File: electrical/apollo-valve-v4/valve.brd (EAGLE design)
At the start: 160 x 100 mm, 42 parts, among them J1 VALVE2, J2 VALVE1, J7 455-1750-1-ND, U1 DRV8806-SSOP, U2 DRV8806-SSOP, U3 TPS54202

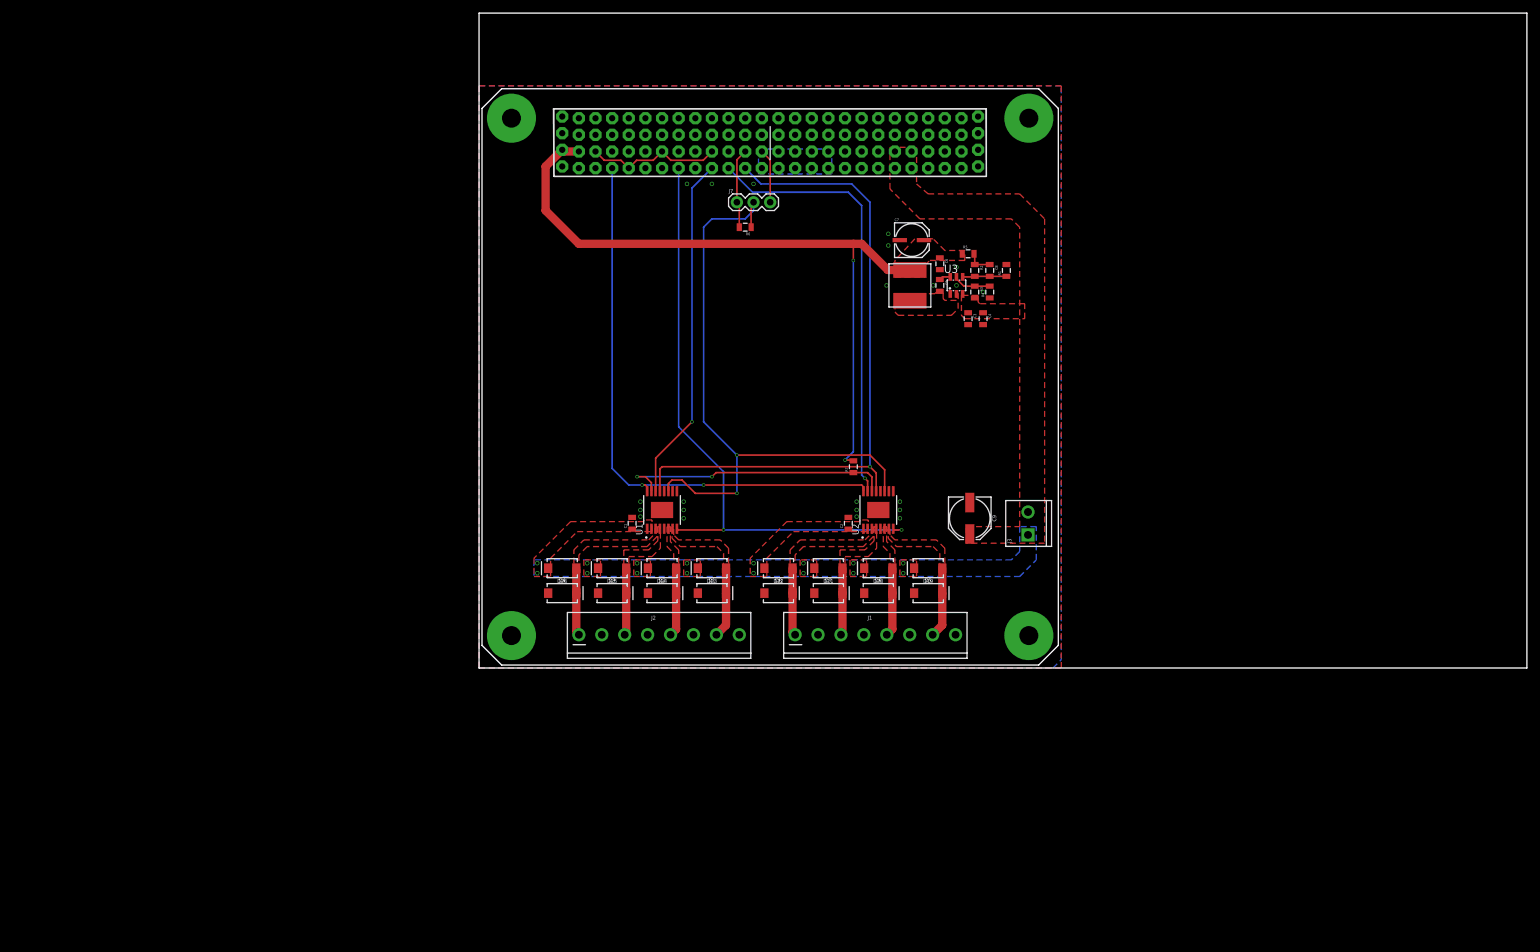
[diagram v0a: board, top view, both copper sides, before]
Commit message: Add stepper drivers to the valve board schematic. No guarantee that they fit, but if they do not another board can be made.
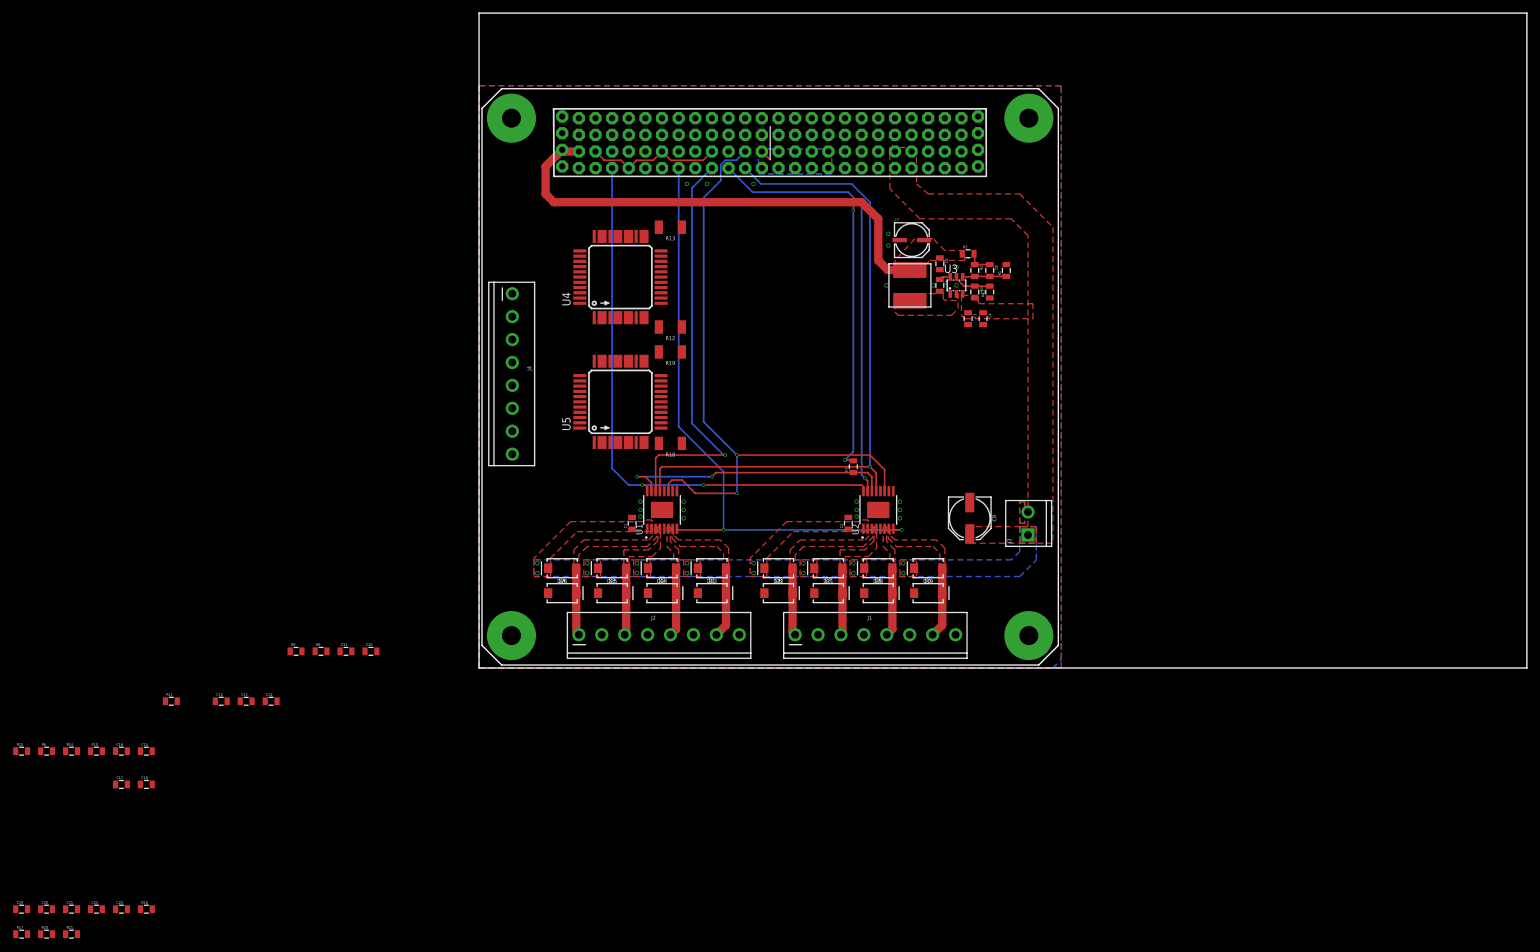
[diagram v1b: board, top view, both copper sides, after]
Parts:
- removed J7: 455-1750-1-ND, SparkFun-Connectors:1X03
- added C10, C11, C13, C14, C17, C18, C20, C21: 0.1u, apollo-ctrl-v4:0805
- added C12, C19: 10u, apollo-ctrl-v4:0805
- added C15, C16, C22, C23: 0.01u, apollo-ctrl-v4:0805
- added J4: STEP, SparkFun-Connectors:SCREWTERMINAL-3.5MM-8
- added R10, R14, R20, R21: 22, apollo-ctrl-v4:0805
- added R11: 13.3K, apollo-ctrl-v4:0805
- added R12, R13, R18, R19: 0.1, SparkFun-Resistors:1210
- added R15, R16, R17, R8, R9: 100K, apollo-ctrl-v4:0805
- added U4, U5: TMC2660, apollo-ctrl-v4:TMC2660
- R3: value 680K -> 499K
- R4: value 120K -> 82K
- moved R6 133.4 mm to (-66.0, -12.7), turned to 0 degrees
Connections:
- removed net LCS: J7.2, R6.1, U1.11, U2.11
- new net +12V: C12.1, C13.1, C14.1, C19.1, C20.1, C21.1, U4.30, U4.35, U4.36, U4.4, U5.30, U5.35, U5.36, U5.4
- new net +3V3: C11.1, C18.1, R15.2, R6.2, U$1.P$1, U4.40, U5.40
- new net 5VOUT1: C10.1, U4.13
- new net 5VOUT2: C17.1, U5.13
- new net BRA1: R10.2, R12.2, U4.9
- new net BRA2: R18.2, R20.2, U5.9
- new net BRB1: R13.2, R14.2, U4.25
- new net BRB2: R19.2, R21.2, U5.25
- new net DIR1: R8.2, U4.41
- new net DIR2: R16.2, U5.41
- new net RESET: R11.1, U1.9, U2.9
- new net S1A: J4.4, U4.2, U4.7
- new net S1B: J4.3, U4.10, U4.5
- new net S1C: J4.2, U4.26, U4.31
- new net S1D: J4.1, U4.23, U4.28
- new net S2A: J4.8, U5.2, U5.7
- new net S2B: J4.7, U5.10, U5.5
- new net S2C: J4.6, U5.26, U5.31
- new net S2D: J4.5, U5.23, U5.28
- new net SRA1: C15.1, R10.1, U4.12
- new net SRA2: C22.1, R20.1, U5.12
- new net SRB1: C16.1, R14.1, U4.22
- new net SRB2: C23.1, R21.1, U5.22
- new net STEP1: R9.2, U4.42
- new net STEP2: R17.2, U5.42
- net !LOE!: now also U4.19, U5.19
- net CIDO: now also U4.14, U5.14
- net CODI: now also U4.15, U5.15
- net CS1: now also U1.11, U2.11; no longer J7.1, R6.2
- net CS2: now also R6.1, U4.18; no longer J7.3
- net CS3: now also R15.1, U5.18
- net GND: now also C10.2, C11.2, C12.2, C13.2, C14.2, C15.2, C16.2, C17.2, C18.2, C19.2, C20.2, C21.2, C22.2, C23.2, R11.2, R12.1, R13.1, R16.1, R17.1, R18.1, R19.1, R8.1, R9.1, U4.17, U4.21, U4.39, U4.43, U4.44, U5.17, U5.21, U5.39, U5.43, U5.44
- net SCK: now also U4.16, U5.16
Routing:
- net LCS: track 96.1 -> 0.00 mm, vias 2 -> 0
- net CS1: track 12.2 -> 96.2 mm, vias 0 -> 2
- net CODI: track 52.9 -> 63.2 mm
- net +5V: track 107.2 -> 115.8 mm
- net CS2: track 8.28 -> 1.80 mm

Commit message: Remove the Trinamics bipolar stepper drivers and add unipolar stepper drivers instead (as the motors are cheaper and more available).
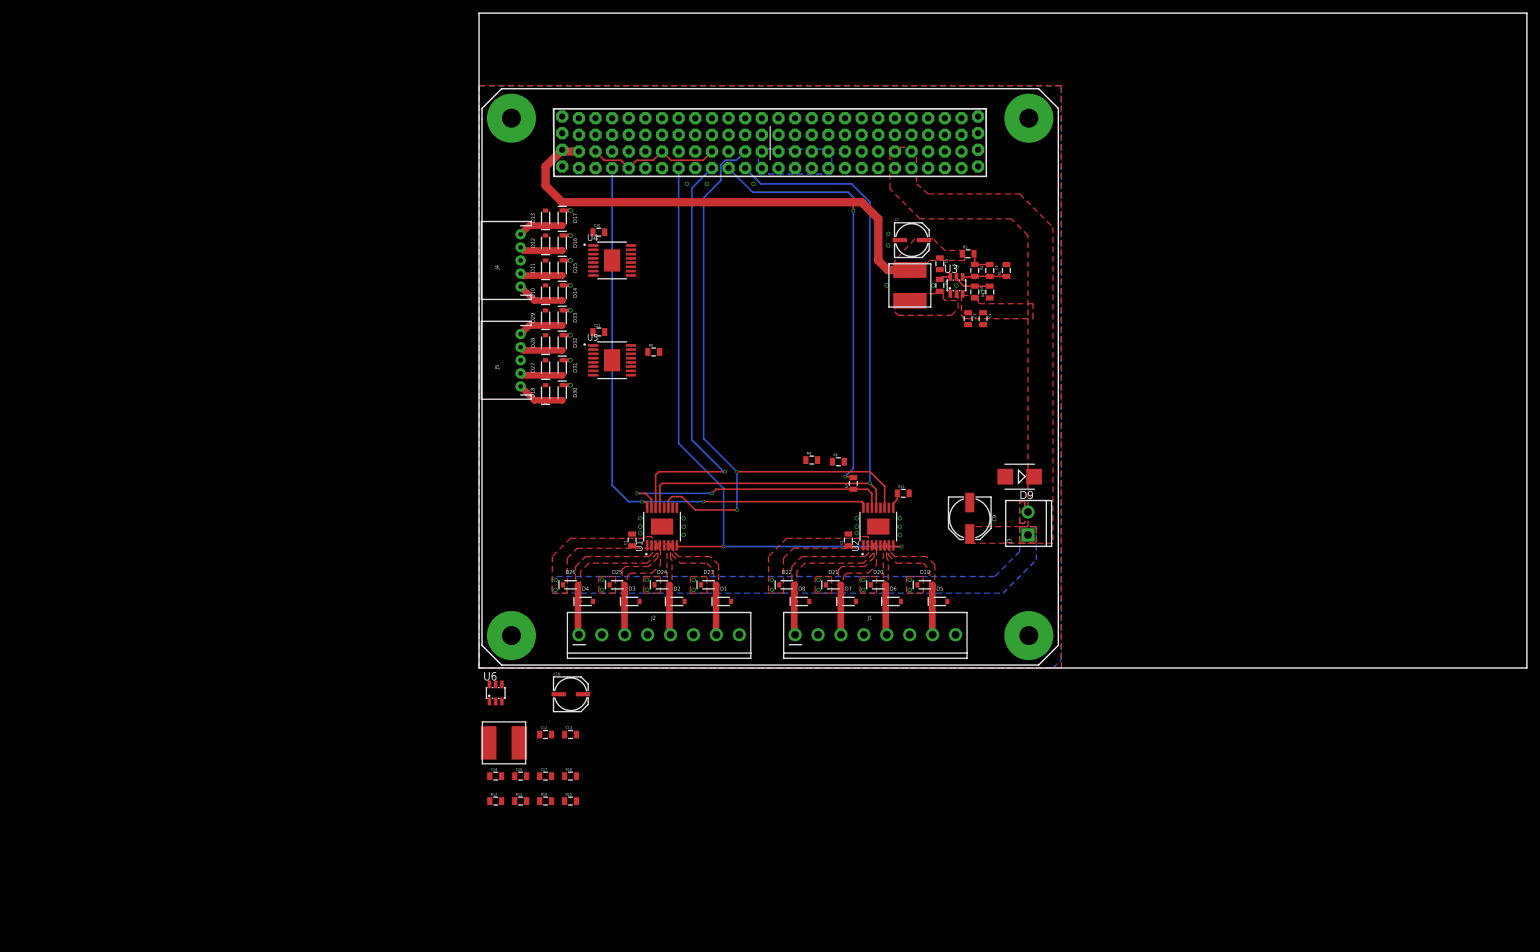
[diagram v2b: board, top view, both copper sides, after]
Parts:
- removed C18, C20, C21: 0.1u, apollo-ctrl-v4:0805
- removed C19: 10u, apollo-ctrl-v4:0805
- removed C22, C23: 0.01u, apollo-ctrl-v4:0805
- removed R16, R17: 100K, apollo-ctrl-v4:0805
- removed R18, R19: 0.1, SparkFun-Resistors:1210
- removed R20, R21: 22, apollo-ctrl-v4:0805
- added D10, D11, D12, D13, D14, D15, D16, D17, D18, D27, D28, D29, D30, D31, D32, D33: BAT46, SparkFun-DiscreteSemi:SOD-323
- added D9: SMBJ24A, diode:SMB
- added J5: S2, SparkFun-Connectors:JST-5-PTH
- added L2: VLS6045EX-220M, apollo-ctrl-v4:VLS6045EX
- added U6: TPS54202, apollo-ctrl-v4:SOT23-6L
- C12: value 10u -> 0.1u
- C13: value 0.1u -> 10u
- C15: value 0.01u -> 22u
- C16: value 0.01u -> 47u; device apollo-ctrl-v4:0805 -> apollo-ctrl-v4:PANASONIC_C
- C17: value 0.1u -> 100p
- D1, D19, D2, D20, D21, D22, D23, D24, D25, D26, D3, D4, D5, D6, D7, D8: value B340A -> BAT46; device SparkFun-DiscreteSemi:SMA-DIODE -> SparkFun-DiscreteSemi:SOD-323
- J4: value STEP -> S1; device SparkFun-Connectors:SCREWTERMINAL-3.5MM-8 -> SparkFun-Connectors:JST-5-PTH
- L1: value VLS6045EX-H -> VLS6045EX-150M
- R10: value 22 -> 5.23K
- R11: value 13.3K -> 2.2K
- R12: value 0.1 -> 100K; device SparkFun-Resistors:1210 -> apollo-ctrl-v4:0805
- R13: value 0.1 -> 499K; device SparkFun-Resistors:1210 -> apollo-ctrl-v4:0805
- R14: value 22 -> 82K
- R15: value 100K -> 49.9
- R6, R7, R8: value 100K -> 2.2K
- R9: value 100K -> EMPTY
- U4, U5: value TMC2660 -> DRV8806-SSOP; device apollo-ctrl-v4:TMC2660 -> apollo-ctrl-v4:SOP65P640X120-17N
- moved R6 128.7 mm to (54.9, 31.5)
- moved R11 116.2 mm to (64.8, 26.7)
- moved R13 90.6 mm to (6.35, -20.3), turned to 0 degrees
- moved R15 84.2 mm to (14.0, -20.3)
- moved R9 84.0 mm to (50.8, 31.8)
- moved R12 77.1 mm to (2.54, -20.3), turned to 0 degrees
- moved C10 72.9 mm to (18.3, 66.5)
- moved R14 72.8 mm to (10.2, -20.3)
- moved R10 72.5 mm to (14.0, -16.5)
- moved C16 69.2 mm to (14.0, -3.81)
- moved R8 68.3 mm to (26.7, 48.3)
- moved C17 64.8 mm to (10.2, -16.5)
- moved C11 62.2 mm to (18.3, 51.3)
- moved C15 57.3 mm to (6.35, -16.5)
- moved C13 49.8 mm to (14.0, -10.2)
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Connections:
- net VEN renamed VEN1
- removed net 5VOUT1: C10.1, U4.13
- removed net 5VOUT2: C17.1, U5.13
- removed net BRA1: R10.2, R12.2, U4.9
- removed net BRA2: R18.2, R20.2, U5.9
- removed net BRB1: R13.2, R14.2, U4.25
- removed net BRB2: R19.2, R21.2, U5.25
- removed net DIR1: R8.2, U4.41
- removed net DIR2: R16.2, U5.41
- removed net SRA1: C15.1, R10.1, U4.12
- removed net SRA2: C22.1, R20.1, U5.12
- removed net SRB1: C16.1, R14.1, U4.22
- removed net SRB2: C23.1, R21.1, U5.22
- removed net STEP1: R9.2, U4.42
- removed net STEP2: R17.2, U5.42
- new net BOOT2: C14.1, U6.6
- new net CIDO2: R6.1, R9.2, U2.15, U4.14
- new net CIDO3: R8.1, U4.15, U5.14
- new net FB2: C17.2, R10.1, R12.2, U6.4
- new net FF2: C17.1, R12.1, R15.2
- new net SW2: C14.2, L2.1, U6.2
- new net VEN2: R13.1, R14.2, U6.5
- net !FAULT!: now also U4.16, U5.16
- net !LOE!: now also U4.8, U5.8; no longer U4.19, U5.19
- net +12V: now also C10.1, C11.1, C15.1, C16.+, D14.C, D15.C, D16.C, D17.C, D30.C, D31.C, D32.C, D33.C, L2.2, R15.1, U4.1, U4.2, U5.1, U5.2; no longer C12.1, C13.1, C14.1, C19.1, C20.1, C21.1, U4.30, U4.35, U4.36, U4.4, U5.30, U5.35, U5.36, U5.4
- net +24V: now also C12.1, C13.1, D9.C, R13.2, U6.3
- net +3V3: no longer C11.1, C18.1, R15.2, R6.2, U4.40, U5.40
- net +5V: now also R6.2, R8.2
- net CIDO: now also R9.1, U5.15; no longer U2.15, U4.14, U5.14
- net CODI: no longer U4.15, U5.15
- net CS1: now also U4.11, U5.11
- net CS2: no longer R6.1, U4.18
- net CS3: no longer R15.1, U5.18
- net GND: now also C16.-, D10.A, D11.A, D12.A, D13.A, D18.A, D27.A, D28.A, D29.A, D9.A, J4.3, J5.3, R10.2, R14.1, U4.12, U4.5, U5.12, U5.5, U6.1; no longer C14.2, C16.2, C17.2, C18.2, C19.2, C20.2, C21.2, C22.2, C23.2, R12.1, R13.1, R16.1, R17.1, R18.1, R19.1, R8.1, R9.1, U4.21, U4.39, U4.43, U4.44, U5.21, U5.39, U5.43, U5.44
- net RESET: now also U4.9, U5.9
- net S1A: now also D13.C, D17.A, J4.5, U4.3; no longer J4.4, U4.2, U4.7
- net S1B: now also D12.C, D16.A, J4.4, U4.4; no longer J4.3, U4.10, U4.5
- net S1C: now also D11.C, D15.A, U4.6; no longer U4.26, U4.31
- net S1D: now also D10.C, D14.A, U4.7; no longer U4.23, U4.28
- net S2A: now also D29.C, D33.A, J5.5, U5.3; no longer J4.8, U5.2, U5.7
- net S2B: now also D28.C, D32.A, J5.4, U5.4; no longer J4.7, U5.10, U5.5
- net S2C: now also D27.C, D31.A, J5.2, U5.6; no longer J4.6, U5.26, U5.31
- net S2D: now also D18.C, D30.A, J5.1, U5.7; no longer J4.5, U5.23, U5.28
- net SCK: now also U4.13, U5.13; no longer U4.16, U5.16
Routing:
- net CIDO: track 66.7 -> 22.7 mm, vias 1 -> 0
- net +12V: track 0.00 -> 10.2 mm, vias 0 -> 8
- net S1D: track 0.00 -> 7.23 mm
- net S2D: track 0.00 -> 7.23 mm
- net S2A: track 0.00 -> 6.90 mm
- net S1A: track 0.00 -> 6.90 mm
- net S2B: track 0.00 -> 6.56 mm
- net S1B: track 0.00 -> 6.56 mm
- net S2C: track 0.00 -> 6.48 mm
- net S1C: track 0.00 -> 6.48 mm
- net CS1: track 96.2 -> 99.9 mm
- net VALVE4: track 10.8 -> 7.65 mm
- net VALVE8: track 10.8 -> 7.65 mm
- net VALVE3: track 10.5 -> 7.68 mm
- net VALVE7: track 10.5 -> 7.69 mm
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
